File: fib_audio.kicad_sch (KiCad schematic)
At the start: 58 parts, among them J701 DNP AUDIO-JACK-8P-SMD, J702 SPK_JST_L, J703 SPK_JST_R, K701 BUTTON-4PDTSM-62K-S-V-T/R(SN4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, U701 WM8960CGEFL, X701 24MHz 306020014

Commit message: implemented most of USB and Power Supplies
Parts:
- C703, C704, C705, C706, C707, C708, C709, C710, C711, C712, C713, C714, C716, C717, C718, C719, C723, C724, C725, C726, C727, C728: footprint Capacitor_SMD:C_0603_1608Metric -> Capacitor_SMD:C_0402_1005Metric
- R701, R702, R703, R704, R705, R706, R707, R708, R709, R710: footprint Resistor_SMD:R_0603_1608Metric -> Resistor_SMD:R_0402_1005Metric
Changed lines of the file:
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@@
 			)
 		)
-		(property "Footprint" "Resistor_SMD:R_0603_1608Metric"
+		(property "Footprint" "Resistor_SMD:R_0402_1005Metric"
 			(at 45.72 185.42 0)
 			(effects
@@
 			)
 		)
-		(property "Footprint" "Resistor_SMD:R_0603_1608Metric"
+		(property "Footprint" "Resistor_SMD:R_0402_1005Metric"
 			(at 21.59 77.47 0)
 			(effects
@@
 			)
 		)
-		(property "Footprint" "Capacitor_SMD:C_0603_1608Metric"
+		(property "Footprint" "Capacitor_SMD:C_0402_1005Metric"
 			(at 264.16 110.49 0)
 			(effects
@@
 			)
 		)
-		(property "Footprint" "Resistor_SMD:R_0603_1608Metric"
+		(property "Footprint" "Resistor_SMD:R_0402_1005Metric"
 			(at 43.18 69.85 0)
 			(effects
@@
 			)
 		)
-		(property "Footprint" "Capacitor_SMD:C_0603_1608Metric"
+		(property "Footprint" "Capacitor_SMD:C_0402_1005Metric"
 			(at 194.31 29.21 0)
 			(effects
@@
 			)
 		)
-		(property "Footprint" "Capacitor_SMD:C_0603_1608Metric"
+		(property "Footprint" "Capacitor_SMD:C_0402_1005Metric"
 			(at 132.08 71.12 0)
 			(effects
@@
 			)
 		)
-		(property "Footprint" "Resistor_SMD:R_0603_1608Metric"
+		(property "Footprint" "Resistor_SMD:R_0402_1005Metric"
 			(at 254 22.225 0)
 			(effects
@@
 			)
 		)
-		(property "Footprint" "Resistor_SMD:R_0603_1608Metric"
+		(property "Footprint" "Resistor_SMD:R_0402_1005Metric"
 			(at 43.18 73.66 0)
 			(effects
@@
 			)
 		)
-		(property "Footprint" "Resistor_SMD:R_0603_1608Metric"
+		(property "Footprint" "Resistor_SMD:R_0402_1005Metric"
 			(at 43.18 66.04 0)
 			(effects
@@
 			)
 		)
-		(property "Footprint" "Capacitor_SMD:C_0603_1608Metric"
+		(property "Footprint" "Capacitor_SMD:C_0402_1005Metric"
 			(at 152.4 29.21 0)
 			(effects
@@
 			)
 		)
-		(property "Footprint" "Capacitor_SMD:C_0603_1608Metric"
+		(property "Footprint" "Capacitor_SMD:C_0402_1005Metric"
 			(at 111.76 53.34 0)
 			(effects
@@
 			)
 		)
-		(property "Footprint" "Capacitor_SMD:C_0603_1608Metric"
+		(property "Footprint" "Capacitor_SMD:C_0402_1005Metric"
 			(at 182.88 29.21 0)
 			(effects
@@
 			)
 		)
-		(property "Footprint" "Capacitor_SMD:C_0603_1608Metric"
+		(property "Footprint" "Capacitor_SMD:C_0402_1005Metric"
 			(at 248.92 110.49 0)
 			(effects
@@
 			)
 		)
-		(property "Footprint" "Capacitor_SMD:C_0603_1608Metric"
+		(property "Footprint" "Capacitor_SMD:C_0402_1005Metric"
 			(at 120.65 53.34 0)
 			(effects
@@
 			)
 		)
-		(property "Footprint" "Capacitor_SMD:C_0603_1608Metric"
+		(property "Footprint" "Capacitor_SMD:C_0402_1005Metric"
 			(at 233.68 110.49 0)
 			(effects
@@
 			)
 		)
-		(property "Footprint" "Resistor_SMD:R_0603_1608Metric"
+		(property "Footprint" "Resistor_SMD:R_0402_1005Metric"
 			(at 26.67 77.47 0)
 			(effects
@@
 			)
 		)
-		(property "Footprint" "Capacitor_SMD:C_0603_1608Metric"
+		(property "Footprint" "Capacitor_SMD:C_0402_1005Metric"
 			(at 52.07 185.42 0)
 			(effects
@@
 			)
 		)
-		(property "Footprint" "Capacitor_SMD:C_0603_1608Metric"
+		(property "Footprint" "Capacitor_SMD:C_0402_1005Metric"
 			(at 248.92 71.12 0)
 			(effects
@@
 			)
 		)
-		(property "Footprint" "Capacitor_SMD:C_0603_1608Metric"
+		(property "Footprint" "Capacitor_SMD:C_0402_1005Metric"
 			(at 120.65 29.21 0)
 			(effects
@@
 			)
 		)
-		(property "Footprint" "Capacitor_SMD:C_0603_1608Metric"
+		(property "Footprint" "Capacitor_SMD:C_0402_1005Metric"
 			(at 132.08 53.34 0)
 			(effects
@@
 			)
 		)
-		(property "Footprint" "Resistor_SMD:R_0603_1608Metric"
+		(property "Footprint" "Resistor_SMD:R_0402_1005Metric"
 			(at 43.18 58.42 0)
 			(effects
@@
 			)
 		)
-		(property "Footprint" "Capacitor_SMD:C_0603_1608Metric"
+		(property "Footprint" "Capacitor_SMD:C_0402_1005Metric"
 			(at 111.76 71.12 0)
 			(effects
@@
 			)
 		)
-		(property "Footprint" "Capacitor_SMD:C_0603_1608Metric"
+		(property "Footprint" "Capacitor_SMD:C_0402_1005Metric"
 			(at 140.97 29.21 0)
 			(effects
@@
 			)
 		)
-		(property "Footprint" "Capacitor_SMD:C_0603_1608Metric"
+		(property "Footprint" "Capacitor_SMD:C_0402_1005Metric"
 			(at 130.81 29.21 0)
 			(effects
@@
 			)
 		)
-		(property "Footprint" "Capacitor_SMD:C_0603_1608Metric"
+		(property "Footprint" "Capacitor_SMD:C_0402_1005Metric"
 			(at 264.16 71.12 0)
 			(effects
@@
 			)
 		)
-		(property "Footprint" "Capacitor_SMD:C_0603_1608Metric"
+		(property "Footprint" "Capacitor_SMD:C_0402_1005Metric"
 			(at 172.72 29.21 0)
 			(effects
@@
 			)
 		)
-		(property "Footprint" "Resistor_SMD:R_0603_1608Metric"
+		(property "Footprint" "Resistor_SMD:R_0402_1005Metric"
 			(at 43.18 62.23 0)
 			(effects
@@
 			)
 		)
-		(property "Footprint" "Capacitor_SMD:C_0603_1608Metric"
+		(property "Footprint" "Capacitor_SMD:C_0402_1005Metric"
 			(at 57.15 185.42 0)
 			(effects
@@
 			)
 		)
-		(property "Footprint" "Capacitor_SMD:C_0603_1608Metric"
+		(property "Footprint" "Capacitor_SMD:C_0402_1005Metric"
 			(at 233.68 71.12 0)
 			(effects
@@
 			)
 		)
-		(property "Footprint" "Capacitor_SMD:C_0603_1608Metric"
+		(property "Footprint" "Capacitor_SMD:C_0402_1005Metric"
 			(at 273.05 128.27 0)
 			(effects
@@
 			)
 		)
-		(property "Footprint" "Capacitor_SMD:C_0603_1608Metric"
+		(property "Footprint" "Capacitor_SMD:C_0402_1005Metric"
 			(at 120.65 71.12 0)
 			(effects
@@
 			)
 		)
-		(property "Footprint" "Resistor_SMD:R_0603_1608Metric"
+		(property "Footprint" "Resistor_SMD:R_0402_1005Metric"
 			(at 39.37 185.42 0)
 			(effects

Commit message: further optimized placement, finished most of buck array, expanded pcie, added tons of missing footprints, diff pair spacing optimization
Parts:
- D701, D702: footprint Untitled:SOD-923 -> Diode_SMD:D_SOD-923
- L701, L702, L707, L708: footprint Untitled:L0603 -> Inductor_SMD:L_0603_1608Metric
- L703, L704, L705, L706: footprint (none) -> Inductor_SMD:L_0603_1608Metric
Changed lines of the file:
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@@
 			)
 		)
-		(property "Footprint" ""
+		(property "Footprint" "Inductor_SMD:L_0603_1608Metric"
 			(at 104.14 64.77 0)
 			(effects
@@
 			)
 		)
-		(property "Footprint" ""
+		(property "Footprint" "Inductor_SMD:L_0603_1608Metric"
 			(at 104.14 67.31 0)
 			(effects
@@
 			)
 		)
-		(property "Footprint" ""
+		(property "Footprint" "Inductor_SMD:L_0603_1608Metric"
 			(at 104.14 49.53 0)
 			(effects
@@
 			)
 		)
-		(property "Footprint" "Untitled:SOD-923"
+		(property "Footprint" "Diode_SMD:D_SOD-923"
 			(at 72.39 184.15 0)
 			(effects
@@
 			)
 		)
-		(property "Footprint" "Untitled:L0603"
+		(property "Footprint" "Inductor_SMD:L_0603_1608Metric"
 			(at 257.81 104.14 0)
 			(effects
@@
 			)
 		)
-		(property "Footprint" "Untitled:L0603"
+		(property "Footprint" "Inductor_SMD:L_0603_1608Metric"
 			(at 78.74 179.07 0)
 			(effects
@@
 			)
 		)
-		(property "Footprint" ""
+		(property "Footprint" "Inductor_SMD:L_0603_1608Metric"
 			(at 104.14 46.99 0)
 			(effects
@@
 			)
 		)
-		(property "Footprint" "Untitled:SOD-923"
+		(property "Footprint" "Diode_SMD:D_SOD-923"
 			(at 64.77 184.15 0)
 			(effects
@@
 			)
 		)
-		(property "Footprint" "Untitled:L0603"
+		(property "Footprint" "Inductor_SMD:L_0603_1608Metric"
 			(at 257.81 64.77 0)
 			(effects
@@
 			)
 		)
-		(property "Footprint" "Untitled:L0603"
+		(property "Footprint" "Inductor_SMD:L_0603_1608Metric"
 			(at 78.74 173.99 0)
 			(effects

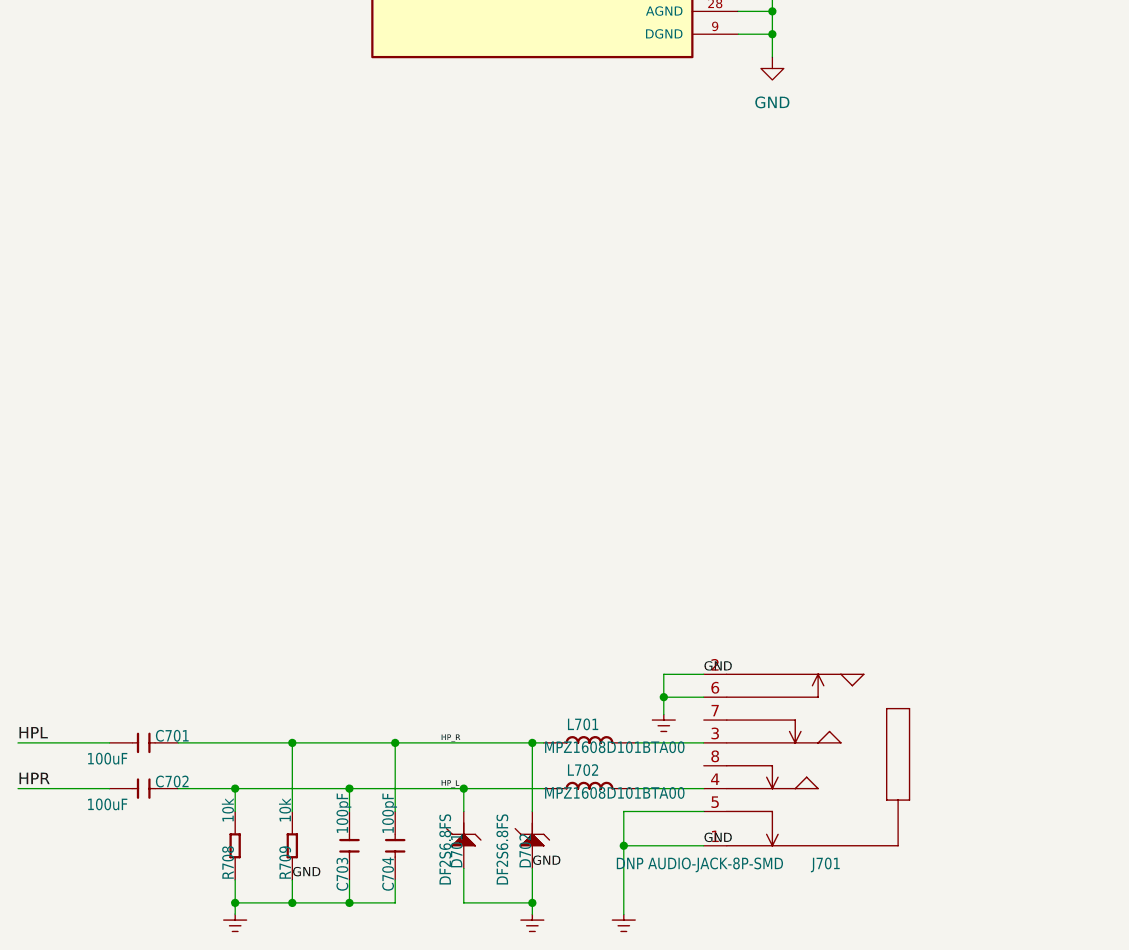
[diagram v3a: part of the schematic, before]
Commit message: replaced 1v8 buck with ldo, added startup circuit, added footprints for eink connectors
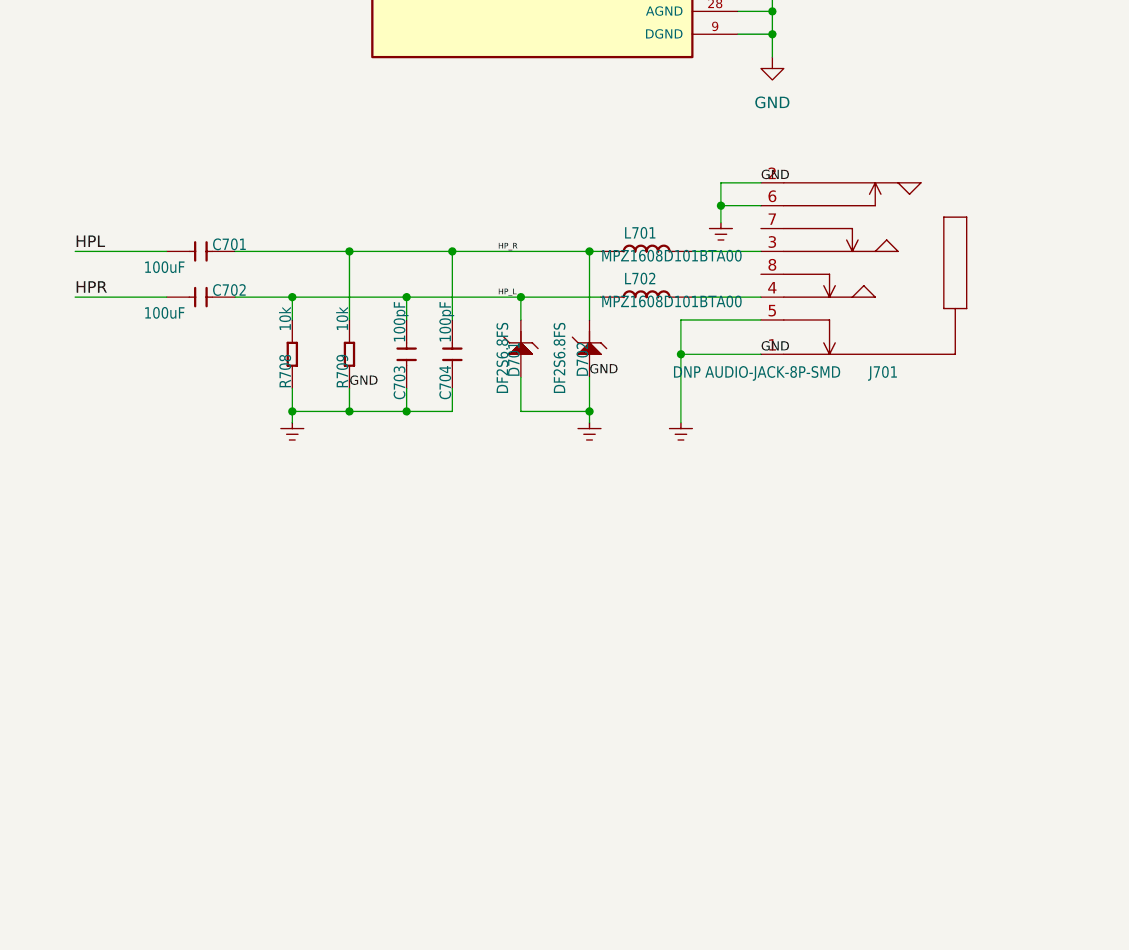
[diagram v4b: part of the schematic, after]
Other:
- moved on the sheet: C701, C702, C703, C704, D701, D702, J701, L701, L702, R708, R709
